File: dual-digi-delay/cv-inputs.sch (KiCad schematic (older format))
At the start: 11 parts, among them J25 DELAY2_CV, J26 DELAY1_CV, SW1 CV_JOIN

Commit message: Final revision of dual digi delay
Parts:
- removed JP1, JP2: Jumper_3_Bridged12, Jumper:SolderJumper-3_P1.3mm_Bridged12_RoundedPad1.0x1.5mm_NumberLabels, symbol Jumper:Jumper_3_Bridged12
- removed R60, R61: 47k, rumblesan-footprints:Resistor_THT_L6.3mm_D2.5mm_P10.16mm_Horizontal, symbol Device:R
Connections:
- net 0V: now also DELAY1_TIME1.3, DELAY2_TIME1.3
- net DELAY1_CV_INPUT: no longer DELAY1_CV_ATTV1.3
- new net DELAY1_CV_CTRL: DELAY1_CV_ATTV1.3
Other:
- moved on the sheet: DELAY1_CV_ATTV1, DELAY2_CV_ATTV1, J25, J26, SW1
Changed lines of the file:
@@
 $Descr A4 11693 8268
 encoding utf-8
-Sheet 7 10
+Sheet 6 10
 Title ""
 Date ""
@@
 L BananaJacks:BananaJack_PanelMount J?
 U 1 1 61A113F4
-P 1750 1650
+P 1350 1050
 AR Path="/61A113F4" Ref="J?"  Part="1"
 AR Path="/619F327A/61A113F4" Ref="J26"  Part="1"
-F 0 "J26" H 1802 1835 50  0000 C CNN
-F 1 "DELAY1_CV" H 1750 1500 50  0000 C CNN
-F 2 "rumblesan-footprints:BananaJack_THT_JohnsonCinch_108-09" H 1750 1350 50  0001 C CNN
-F 3 "" H 1750 1350 50  0001 C CNN
-	1    1750 1650
+F 0 "J26" H 1402 1235 50  0000 C CNN
+F 1 "DELAY1_CV" H 1350 900 50  0000 C CNN
+F 2 "rumblesan-footprints:BananaJack_THT_JohnsonCinch_108-09" H 1350 750 50  0001 C CNN
+F 3 "" H 1350 750 50  0001 C CNN
+	1    1350 1050
 	1    0    0    -1
-$EndComp
-Wire Wire Line
-	2100 1650 2300 1650
-Connection ~ 2100 1650
-Wire Wire Line
-	1950 1650 2100 1650
-$Comp
-L Device:R R?
-U 1 1 61A113FD
-P 2300 1900
-AR Path="/61A113FD" Ref="R?"  Part="1"
-AR Path="/619F327A/61A113FD" Ref="R61"  Part="1"
-F 0 "R61" H 2230 1854 50  0000 R CNN
-F 1 "47k" H 2230 1945 50  0000 R CNN
-F 2 "rumblesan-footprints:Resistor_THT_L6.3mm_D2.5mm_P10.16mm_Horizontal" V 2230 1900 50  0001 C CNN
-F 3 "~" H 2300 1900 50  0001 C CNN
-	1    2300 1900
-	-1   0    0    1
 $EndComp
 $Comp
 L Device:R_POT DELAY1_CV_ATTV?
 U 1 1 61A11403
-P 2100 2200
+P 1700 2800
 AR Path="/61A11403" Ref="DELAY1_CV_ATTV?"  Part="1"
 AR Path="/619F327A/61A11403" Ref="DELAY1_CV_ATTV1"  Part="1"
-F 0 "DELAY1_CV_ATTV1" H 2031 2154 50  0000 R CNN
-F 1 "100kB" H 2031 2245 50  0000 R CNN
-F 2 "rumblesan-footprints:Potentiometer_Alpha_RD901F-40-00D_Single_Vertical_CircularHoles" H 2100 2200 50  0001 C CNN
-F 3 "~" H 2100 2200 50  0001 C CNN
-	1    2100 2200
+F 0 "DELAY1_CV_ATTV1" H 1631 2754 50  0000 R CNN
+F 1 "100kB" H 1631 2845 50  0000 R CNN
+F 2 "rumblesan-footprints:Potentiometer_Alpha_RD901F-40-00D_Single_Vertical_CircularHoles" H 1700 2800 50  0001 C CNN
+F 3 "~" H 1700 2800 50  0001 C CNN
+	1    1700 2800
 	1    0    0    1
 $EndComp
-Wire Wire Line
-	2250 2200 2300 2200
-Wire Wire Line
-	2100 2050 2100 1650
-Wire Wire Line
-	2300 1750 2300 1650
-Wire Wire Line
-	2300 2050 2300 2200
-Connection ~ 2300 1650
-Wire Wire Line
-	2300 1650 2400 1650
-Connection ~ 2300 2200
-Wire Wire Line
-	2300 2200 2400 2200
-Wire Wire Line
-	2100 2350 2100 2550
-Text Label 2100 2550 3    50   ~ 0
-0V
-Text HLabel 2400 1650 2    50   Input ~ 0
+Text HLabel 1750 1050 2    50   Input ~ 0
 DELAY1_CV_INPUT
-Text HLabel 2400 2200 2    50   Input ~ 0
+Text HLabel 2000 2800 2    50   Input ~ 0
 DELAY1_CV_ATTV
 Wire Wire Line
@@
 Wire Wire Line
 	4650 2000 4500 2000
-Wire Wire Line
-	4350 2150 4350 2350
-$Comp
-L Jumper:Jumper_3_Bridged12 JP?
-U 1 1 61A4D9F8
-P 4350 2500
-AR Path="/61A4D9F8" Ref="JP?"  Part="1"
-AR Path="/619F327A/61A4D9F8" Ref="JP2"  Part="1"
-F 0 "JP2" H 4350 2612 50  0000 C CNN
-F 1 "Jumper_3_Bridged12" H 4350 2702 50  0001 C CNN
-F 2 "Jumper:SolderJumper-3_P1.3mm_Bridged12_RoundedPad1.0x1.5mm_NumberLabels" H 4350 2500 50  0001 C CNN
-F 3 "~" H 4350 2500 50  0001 C CNN
-	1    4350 2500
-	-1   0    0    1
-$EndComp
-Wire Wire Line
-	4000 2500 4100 2500
-Wire Wire Line
-	4600 2500 4700 2500
 Text Label 4350 1700 1    50   ~ 0
 -V
-Text Label 4000 2500 2    50   ~ 0
-+V
-Text Label 4700 2500 0    50   ~ 0
+Text Label 4350 2450 3    50   ~ 0
 0V
 Text HLabel 4650 2000 2    50   Input ~ 0
@@
 L BananaJacks:BananaJack_PanelMount J?
 U 1 1 61A9DB63
-P 1350 3950
+P 1350 1550
 AR Path="/61A9DB63" Ref="J?"  Part="1"
 AR Path="/619F327A/61A9DB63" Ref="J25"  Part="1"
-F 0 "J25" H 1402 4135 50  0000 C CNN
-F 1 "DELAY2_CV" H 1350 3800 50  0000 C CNN
-F 2 "rumblesan-footprints:BananaJack_THT_JohnsonCinch_108-09" H 1350 3650 50  0001 C CNN
-F 3 "" H 1350 3650 50  0001 C CNN
-	1    1350 3950
+F 0 "J25" H 1402 1735 50  0000 C CNN
+F 1 "DELAY2_CV" H 1350 1400 50  0000 C CNN
+F 2 "rumblesan-footprints:BananaJack_THT_JohnsonCinch_108-09" H 1350 1250 50  0001 C CNN
+F 3 "" H 1350 1250 50  0001 C CNN
+	1    1350 1550
 	1    0    0    -1
 $EndComp
@@
 L Switch:SW_SPST SW?
 U 1 1 61A9DB69
-P 2350 3400
+P 2150 4150
 AR Path="/61A9DB69" Ref="SW?"  Part="1"
 AR Path="/619F327A/61A9DB69" Ref="SW1"  Part="1"
-F 0 "SW1" H 2350 3635 50  0000 C CNN
-F 1 "CV_JOIN" H 2350 3544 50  0000 C CNN
-F 2 "rumblesan-footprints:Toggle_Switch_100SP1T1B3M2QE" H 2350 3400 50  0001 C CNN
-F 3 "~" H 2350 3400 50  0001 C CNN
-	1    2350 3400
+F 0 "SW1" H 2150 4385 50  0000 C CNN
+F 1 "CV_JOIN" H 2150 4294 50  0000 C CNN
+F 2 "rumblesan-footprints:Toggle_Switch_100SP1T1B3M2QE" H 2150 4150 50  0001 C CNN
+F 3 "~" H 2150 4150 50  0001 C CNN
+	1    2150 4150
 	1    0    0    -1
 $EndComp
 Wire Wire Line
-	1550 3950 1700 3950
+	2350 4150 2500 4150
 Wire Wire Line
-	2550 3400 2700 3400
-Wire Wire Line
-	1750 5400 1850 5400
-Wire Wire Line
-	1600 5550 1600 5700
+	1800 5150 1800 5300
 $Comp
 L Device:R_POT DELAY2_CV_ATTV?
 U 1 1 61A9DB79
-P 1600 5400
+P 1800 5000
 AR Path="/61A9DB79" Ref="DELAY2_CV_ATTV?"  Part="1"
 AR Path="/619F327A/61A9DB79" Ref="DELAY2_CV_ATTV1"  Part="1"
-F 0 "DELAY2_CV_ATTV1" H 1531 5354 50  0000 R CNN
-F 1 "100kB" H 1531 5445 50  0000 R CNN
-F 2 "rumblesan-footprints:Potentiometer_Alpha_RD901F-40-00D_Single_Vertical_CircularHoles" H 1600 5400 50  0001 C CNN
-F 3 "~" H 1600 5400 50  0001 C CNN
-	1    1600 5400
+F 0 "DELAY2_CV_ATTV1" H 1731 4954 50  0000 R CNN
+F 1 "100kB" H 1731 5045 50  0000 R CNN
+F 2 "rumblesan-footprints:Potentiometer_Alpha_RD901F-40-00D_Single_Vertical_CircularHoles" H 1800 5000 50  0001 C CNN
+F 3 "~" H 1800 5000 50  0001 C CNN
+	1    1800 5000
 	1    0    0    1
 $EndComp
-$Comp
-L Device:R R?
-U 1 1 61A9DB7F
-P 1850 5150
-AR Path="/61A9DB7F" Ref="R?"  Part="1"
-AR Path="/619F327A/61A9DB7F" Ref="R60"  Part="1"
-F 0 "R60" H 1780 5104 50  0000 R CNN
-F 1 "47k" H 1780 5195 50  0000 R CNN
-F 2 "rumblesan-footprints:Resistor_THT_L6.3mm_D2.5mm_P10.16mm_Horizontal" V 1780 5150 50  0001 C CNN
-F 3 "~" H 1850 5150 50  0001 C CNN
-	1    1850 5150
-	-1   0    0    1
-$EndComp
-Wire Wire Line
-	1850 5000 1850 4900
-Wire Wire Line
-	1850 4900 1600 4900
-Connection ~ 1600 4900
-Wire Wire Line
-	1600 4900 1600 5250
-Wire Wire Line
-	1850 5300 1850 5400
-Connection ~ 1850 5400
 Wire Wire Line
 	4100 4800 4100 4950
@@
 Wire Wire Line
 	4400 5100 4250 5100
-Wire Wire Line
-	4100 5250 4100 5450
-$Comp
-L Jumper:Jumper_3_Bridged12 JP?
-U 1 1 61A9DB96
-P 4100 5600
-AR Path="/61A9DB96" Ref="JP?"  Part="1"
-AR Path="/619F327A/61A9DB96" Ref="JP1"  Part="1"
-F 0 "JP1" H 4100 5712 50  0000 C CNN
-F 1 "Jumper_3_Bridged12" H 4100 5802 50  0001 C CNN
-F 2 "Jumper:SolderJumper-3_P1.3mm_Bridged12_RoundedPad1.0x1.5mm_NumberLabels" H 4100 5600 50  0001 C CNN
-F 3 "~" H 4100 5600 50  0001 C CNN
-	1    4100 5600
-	-1   0    0    1
-$EndComp
-Wire Wire Line
-	3750 5600 3850 5600
-Wire Wire Line
-	4350 5600 4450 5600
-Text HLabel 2000 3400 0    50   Input ~ 0
+Text HLabel 1800 4150 0    50   Input ~ 0
 JOIN_CV_SOURCE
-Text HLabel 2700 3400 2    50   Input ~ 0
+Text HLabel 2500 4150 2    50   Input ~ 0
 JOIN_CV
 Wire Wire Line
-	2150 3400 2000 3400
-Text HLabel 1700 3950 2    50   Input ~ 0
+	1950 4150 1800 4150
+Text HLabel 1750 1550 2    50   Input ~ 0
 DELAY2_CV_INPUT
-Text HLabel 1600 4750 0    50   Input ~ 0
+Text HLabel 1650 4700 0    50   Input ~ 0
 DELAY2_CV_CTRL
-Text Label 1600 5700 3    50   ~ 0
+Text Label 1800 5300 3    50   ~ 0
 0V
-Text HLabel 2000 5400 2    50   Input ~ 0
+Text HLabel 2100 5000 2    50   Input ~ 0
 DELAY2_CV_ATTV
-Wire Wire Line
-	1850 5400 2000 5400
-Text Label 4450 5600 0    50   ~ 0
+Text Label 4100 5550 3    50   ~ 0
 0V
 Text Label 4100 4800 1    50   ~ 0
 -V
-Text Label 3750 5600 2    50   ~ 0
-+V
 Text HLabel 4400 5100 2    50   Input ~ 0
 DELAY2_CONTROL
@@
 Wire Wire Line
 	4100 3600 4250 3600
-Wire Wire Line
-	4250 3500 4100 3500
 Text HLabel 4100 3700 0    50   Input ~ 0
 -V
 Text HLabel 4100 3600 0    50   Input ~ 0
 0V
-Text HLabel 4100 3500 0    50   Input ~ 0
-+V
 Text Label 4250 3600 0    50   ~ 0
 0V
 Text Label 4250 3700 0    50   ~ 0
 -V
-Text Label 4250 3500 0    50   ~ 0
-+V
 Wire Wire Line
-	1600 4750 1600 4900
+	4100 5250 4100 5550
+Wire Wire Line
+	4350 2150 4350 2450
+Wire Wire Line
+	1700 2950 1700 3100
+Text Label 1700 3100 3    50   ~ 0
+0V
+Wire Wire Line
+	1550 1050 1750 1050
+Wire Wire Line
+	1550 1550 1750 1550
+Text HLabel 1550 2500 0    50   Input ~ 0
+DELAY1_CV_CTRL
+Wire Wire Line
+	1550 2500 1700 2500
+Wire Wire Line
+	1700 2500 1700 2650
+Wire Wire Line
+	1850 2800 2000 2800
+Wire Wire Line
+	1650 4700 1800 4700
+Wire Wire Line
+	1800 4700 1800 4850
+Wire Wire Line
+	1950 5000 2100 5000
 $EndSCHEMATC

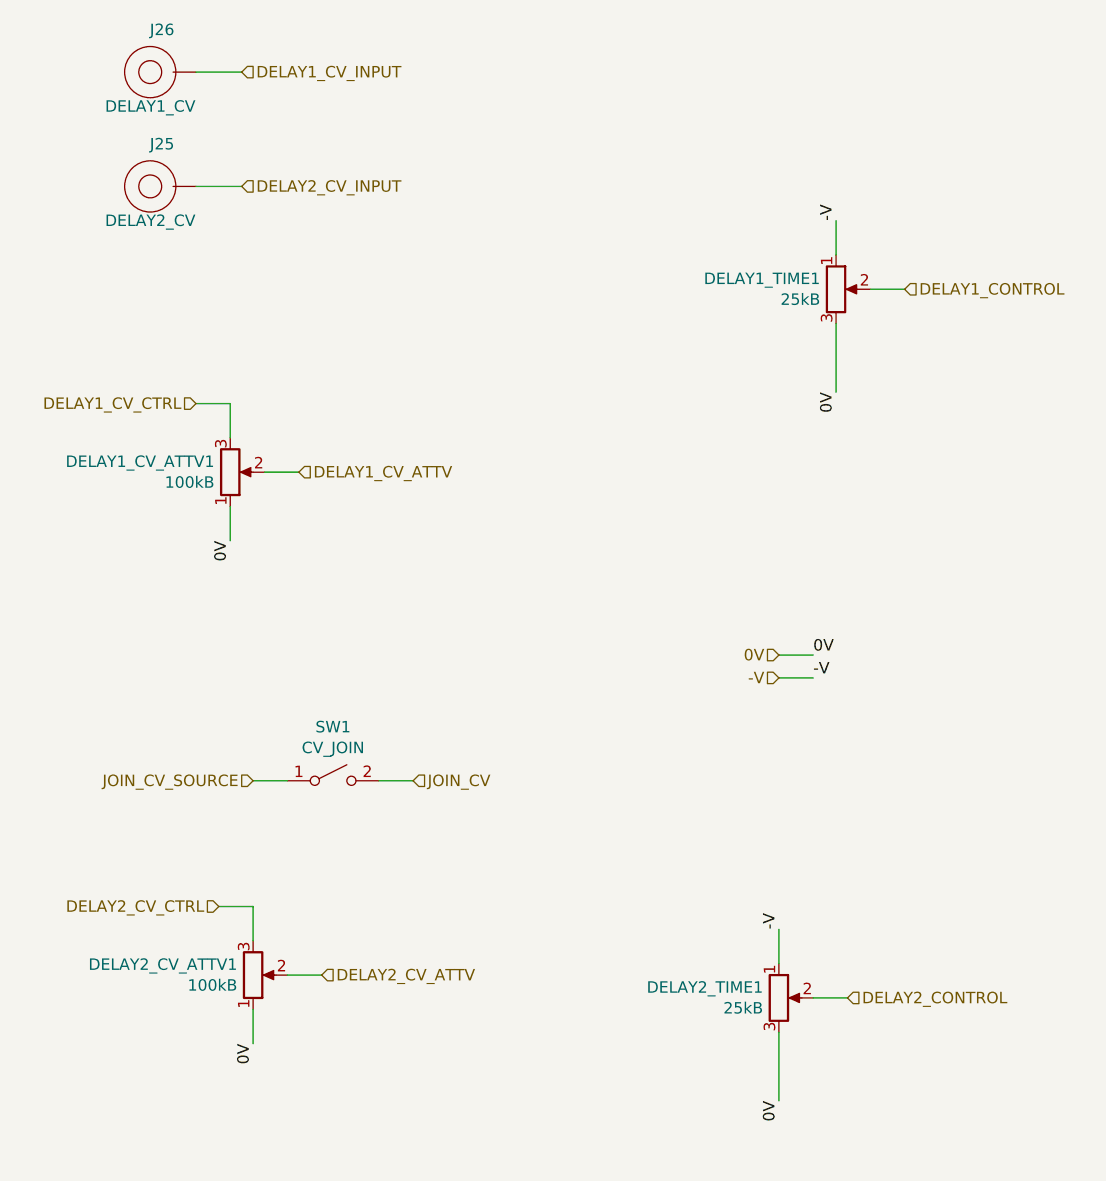
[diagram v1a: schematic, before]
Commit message: Updating digi delay to rev 2
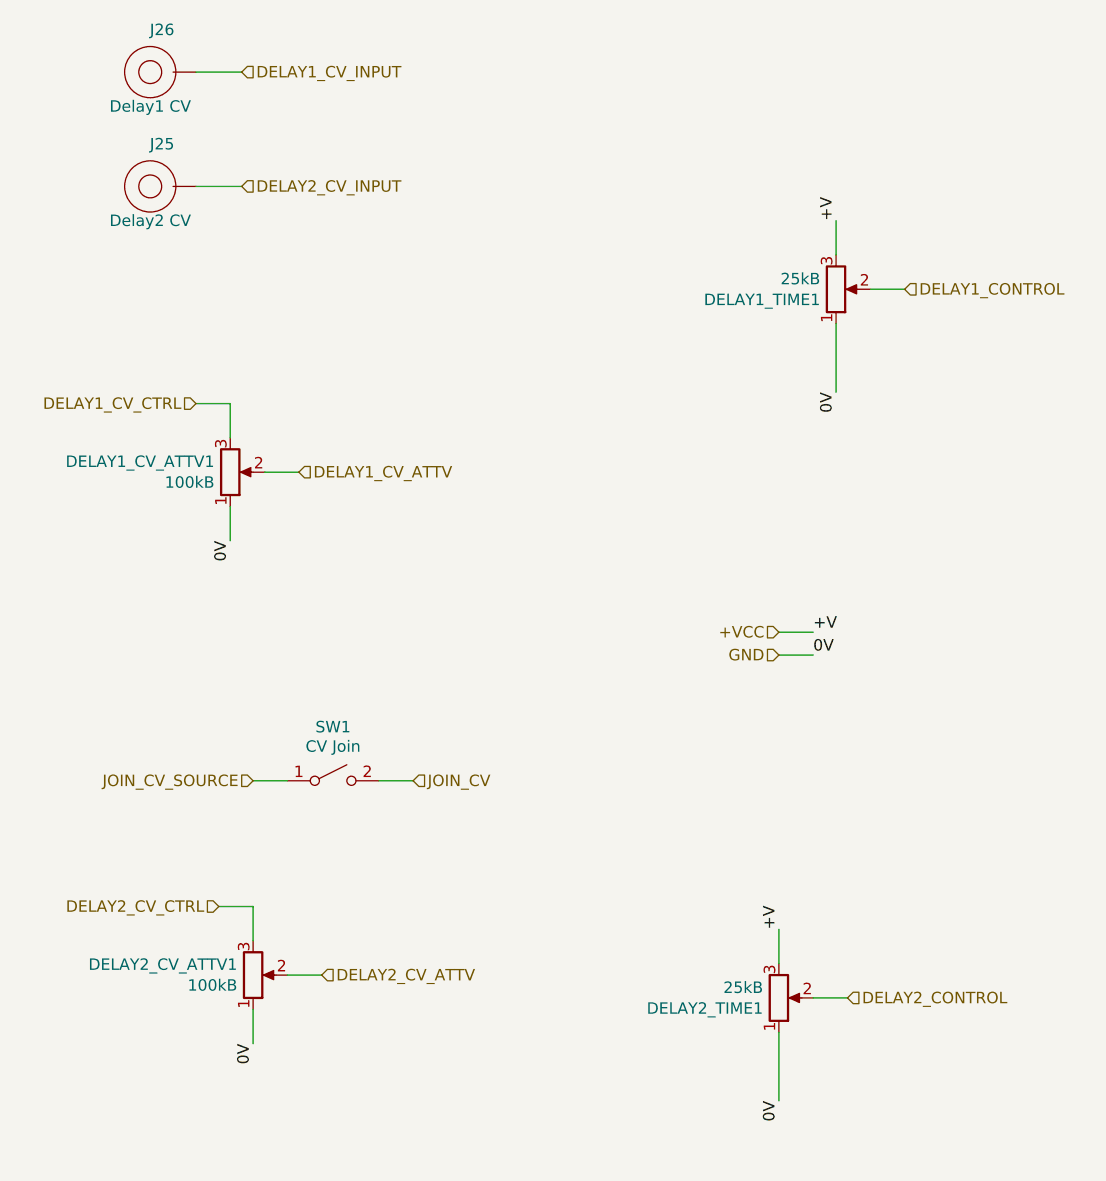
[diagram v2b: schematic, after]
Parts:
- DELAY1_CV_ATTV1, DELAY1_TIME1, DELAY2_CV_ATTV1, DELAY2_TIME1: Vendor (none) -> Thonk
- J25: value DELAY2_CV -> BananaJack_PanelMount; Note (none) -> Delay2 CV; SKU (none) -> 108-0901-1; Vendor (none) -> Mouser
- J26: value DELAY1_CV -> BananaJack_PanelMount; Note (none) -> Delay1 CV; SKU (none) -> 108-0901-1; Vendor (none) -> Mouser
- SW1: value CV_JOIN -> SW_SPST; Note (none) -> CV Join; SKU (none) -> 612-100SP1T1B3M2QEH; Vendor (none) -> Mouser
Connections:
- net -V renamed GND
- net GND: now also DELAY1_CV_ATTV1.1, DELAY2_CV_ATTV1.1
- net 0V renamed +VCC
- net +VCC: no longer DELAY1_CV_ATTV1.1, DELAY2_CV_ATTV1.1
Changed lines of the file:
@@
 $Descr A4 11693 8268
 encoding utf-8
-Sheet 6 10
+Sheet 6 11
 Title ""
 Date ""
@@
 AR Path="/619F327A/61A113F4" Ref="J26"  Part="1"
 F 0 "J26" H 1402 1235 50  0000 C CNN
-F 1 "DELAY1_CV" H 1350 900 50  0000 C CNN
+F 1 "BananaJack_PanelMount" H 1350 1275 50  0001 C CNN
 F 2 "rumblesan-footprints:BananaJack_THT_JohnsonCinch_108-09" H 1350 750 50  0001 C CNN
 F 3 "" H 1350 750 50  0001 C CNN
+F 4 "108-0901-1" H 1350 1350 50  0001 C CNN "SKU"
+F 5 "Mouser" H 1350 1425 50  0001 C CNN "Vendor"
+F 6 "Delay1 CV" H 1350 900 50  0000 C CNN "Note"
 	1    1350 1050
 	1    0    0    -1
-$EndComp
-$Comp
-L Device:R_POT DELAY1_CV_ATTV?
-U 1 1 61A11403
-P 1700 2800
-AR Path="/61A11403" Ref="DELAY1_CV_ATTV?"  Part="1"
-AR Path="/619F327A/61A11403" Ref="DELAY1_CV_ATTV1"  Part="1"
-F 0 "DELAY1_CV_ATTV1" H 1631 2754 50  0000 R CNN
-F 1 "100kB" H 1631 2845 50  0000 R CNN
-F 2 "rumblesan-footprints:Potentiometer_Alpha_RD901F-40-00D_Single_Vertical_CircularHoles" H 1700 2800 50  0001 C CNN
-F 3 "~" H 1700 2800 50  0001 C CNN
-	1    1700 2800
-	1    0    0    1
 $EndComp
 Text HLabel 1750 1050 2    50   Input ~ 0
@@
 Wire Wire Line
 	4350 1700 4350 1850
-$Comp
-L Device:R_POT DELAY1_TIME?
-U 1 1 61A4D9F0
-P 4350 2000
-AR Path="/61A4D9F0" Ref="DELAY1_TIME?"  Part="1"
-AR Path="/619F327A/61A4D9F0" Ref="DELAY1_TIME1"  Part="1"
-F 0 "DELAY1_TIME1" H 4281 2046 50  0000 R CNN
-F 1 "25kB" H 4281 1955 50  0000 R CNN
-F 2 "rumblesan-footprints:Potentiometer_Alpha_RD901F-40-00D_Single_Vertical_CircularHoles" H 4350 2000 50  0001 C CNN
-F 3 "~" H 4350 2000 50  0001 C CNN
-	1    4350 2000
-	1    0    0    -1
-$EndComp
 Wire Wire Line
 	4650 2000 4500 2000
-Text Label 4350 1700 1    50   ~ 0
--V
 Text Label 4350 2450 3    50   ~ 0
 0V
@@
 AR Path="/619F327A/61A9DB63" Ref="J25"  Part="1"
 F 0 "J25" H 1402 1735 50  0000 C CNN
-F 1 "DELAY2_CV" H 1350 1400 50  0000 C CNN
+F 1 "BananaJack_PanelMount" H 1350 1775 50  0001 C CNN
 F 2 "rumblesan-footprints:BananaJack_THT_JohnsonCinch_108-09" H 1350 1250 50  0001 C CNN
 F 3 "" H 1350 1250 50  0001 C CNN
+F 4 "108-0901-1" H 1350 1850 50  0001 C CNN "SKU"
+F 5 "Mouser" H 1350 1925 50  0001 C CNN "Vendor"
+F 6 "Delay2 CV" H 1350 1400 50  0000 C CNN "Note"
 	1    1350 1550
 	1    0    0    -1
@@
 AR Path="/619F327A/61A9DB69" Ref="SW1"  Part="1"
 F 0 "SW1" H 2150 4385 50  0000 C CNN
-F 1 "CV_JOIN" H 2150 4294 50  0000 C CNN
+F 1 "SW_SPST" H 2150 4294 50  0001 C CNN
 F 2 "rumblesan-footprints:Toggle_Switch_100SP1T1B3M2QE" H 2150 4150 50  0001 C CNN
 F 3 "~" H 2150 4150 50  0001 C CNN
+F 4 "Mouser" H 2150 4150 50  0001 C CNN "Vendor"
+F 5 "612-100SP1T1B3M2QEH" H 2150 4150 50  0001 C CNN "SKU"
+F 6 "CV Join" H 2150 4300 50  0000 C CNN "Note"
 	1    2150 4150
 	1    0    0    -1
@@
 F 2 "rumblesan-footprints:Potentiometer_Alpha_RD901F-40-00D_Single_Vertical_CircularHoles" H 1800 5000 50  0001 C CNN
 F 3 "~" H 1800 5000 50  0001 C CNN
+F 4 "Thonk" H 1800 5000 50  0001 C CNN "Vendor"
 	1    1800 5000
 	1    0    0    1
@@
 Wire Wire Line
 	4100 4800 4100 4950
-$Comp
-L Device:R_POT DELAY2_TIME?
-U 1 1 61A9DB8E
-P 4100 5100
-AR Path="/61A9DB8E" Ref="DELAY2_TIME?"  Part="1"
-AR Path="/619F327A/61A9DB8E" Ref="DELAY2_TIME1"  Part="1"
-F 0 "DELAY2_TIME1" H 4031 5146 50  0000 R CNN
-F 1 "25kB" H 4031 5055 50  0000 R CNN
-F 2 "rumblesan-footprints:Potentiometer_Alpha_RD901F-40-00D_Single_Vertical_CircularHoles" H 4100 5100 50  0001 C CNN
-F 3 "~" H 4100 5100 50  0001 C CNN
-	1    4100 5100
-	1    0    0    -1
-$EndComp
 Wire Wire Line
 	4400 5100 4250 5100
@@
 Text Label 4100 5550 3    50   ~ 0
 0V
-Text Label 4100 4800 1    50   ~ 0
--V
 Text HLabel 4400 5100 2    50   Input ~ 0
 DELAY2_CONTROL
 Wire Wire Line
-	4250 3700 4100 3700
+	4250 3500 4100 3500
 Wire Wire Line
 	4100 3600 4250 3600
-Text HLabel 4100 3700 0    50   Input ~ 0
--V
 Text HLabel 4100 3600 0    50   Input ~ 0
-0V
+GND
 Text Label 4250 3600 0    50   ~ 0
 0V
-Text Label 4250 3700 0    50   ~ 0
--V
 Wire Wire Line
 	4100 5250 4100 5550
@@
 Wire Wire Line
 	1950 5000 2100 5000
+Text HLabel 4100 3500 0    50   Input ~ 0
++VCC
+Text Label 4250 3500 0    50   ~ 0
++V
+Text Label 4350 1700 1    50   ~ 0
++V
+Text Label 4100 4800 1    50   ~ 0
++V
+$Comp
+L Device:R_POT DELAY1_CV_ATTV?
+U 1 1 61A11403
+P 1700 2800
+AR Path="/61A11403" Ref="DELAY1_CV_ATTV?"  Part="1"
+AR Path="/619F327A/61A11403" Ref="DELAY1_CV_ATTV1"  Part="1"
+F 0 "DELAY1_CV_ATTV1" H 1631 2754 50  0000 R CNN
+F 1 "100kB" H 1631 2845 50  0000 R CNN
+F 2 "rumblesan-footprints:Potentiometer_Alpha_RD901F-40-00D_Single_Vertical_CircularHoles" H 1700 2800 50  0001 C CNN
+F 3 "~" H 1700 2800 50  0001 C CNN
+F 4 "Thonk" H 1700 2800 50  0001 C CNN "Vendor"
+	1    1700 2800
+	1    0    0    1
+$EndComp
+$Comp
+L Device:R_POT DELAY1_TIME?
+U 1 1 61A4D9F0
+P 4350 2000
+AR Path="/61A4D9F0" Ref="DELAY1_TIME?"  Part="1"
+AR Path="/619F327A/61A4D9F0" Ref="DELAY1_TIME1"  Part="1"
+F 0 "DELAY1_TIME1" H 4281 2046 50  0000 R CNN
+F 1 "25kB" H 4281 1955 50  0000 R CNN
+F 2 "rumblesan-footprints:Potentiometer_Alpha_RD901F-40-00D_Single_Vertical_CircularHoles" H 4350 2000 50  0001 C CNN
+F 3 "~" H 4350 2000 50  0001 C CNN
+F 4 "Thonk" H 4350 2000 50  0001 C CNN "Vendor"
+	1    4350 2000
+	1    0    0    1
+$EndComp
+$Comp
+L Device:R_POT DELAY2_TIME?
+U 1 1 61A9DB8E
+P 4100 5100
+AR Path="/61A9DB8E" Ref="DELAY2_TIME?"  Part="1"
+AR Path="/619F327A/61A9DB8E" Ref="DELAY2_TIME1"  Part="1"
+F 0 "DELAY2_TIME1" H 4031 5146 50  0000 R CNN
+F 1 "25kB" H 4031 5055 50  0000 R CNN
+F 2 "rumblesan-footprints:Potentiometer_Alpha_RD901F-40-00D_Single_Vertical_CircularHoles" H 4100 5100 50  0001 C CNN
+F 3 "~" H 4100 5100 50  0001 C CNN
+F 4 "Thonk" H 4100 5100 50  0001 C CNN "Vendor"
+	1    4100 5100
+	1    0    0    1
+$EndComp
 $EndSCHEMATC
